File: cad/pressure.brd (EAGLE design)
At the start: 47.9 x 64.8 mm, 14 parts, among them U1 WEMOS-D1-MINI, U2 ABPSENSOR, U3 BATTERY-CHARGER-LI-PROT

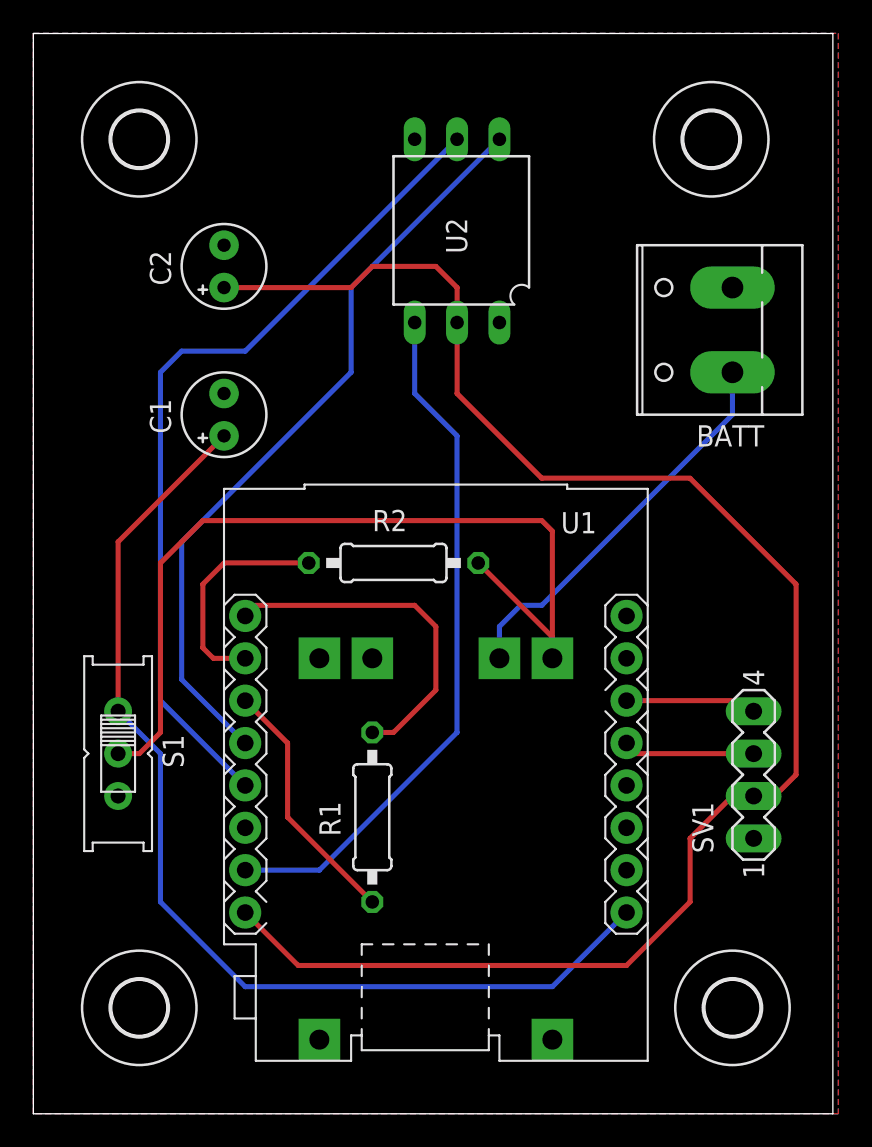
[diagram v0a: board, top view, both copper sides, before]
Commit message: Added pressure sensor settings to status
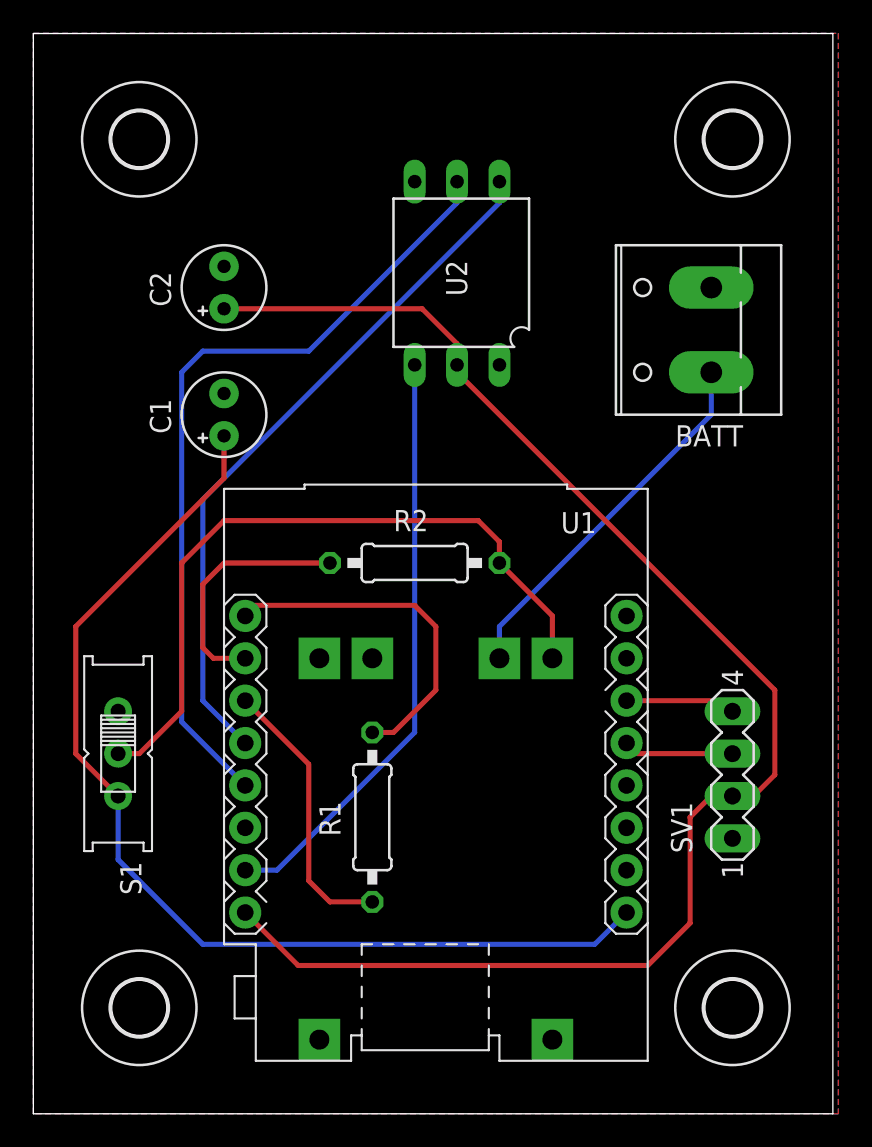
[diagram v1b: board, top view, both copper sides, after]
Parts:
- moved U2 2.54 mm to (38.1, 53.3)
- moved BATT 1.27 mm to (52.1, 48.3)
- moved C2 1.27 mm to (22.9, 50.8)
- moved U$3 1.27 mm to (53.3, 59.7)
- moved R2 1.27 mm to (34.3, 34.3)
- moved SV1 1.27 mm to (53.3, 21.6)
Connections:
- net +5V: now also S1.S; no longer S1.O
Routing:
- net N$10: track 53.2 -> 42.7 mm
- net +3V3: track 99.2 -> 90.1 mm
- net N$4: track 41.7 -> 35.6 mm
- net N$2: track 45.7 -> 42.1 mm
- net N$1: track 50.4 -> 48.3 mm
- net N$6: track 15.2 -> 16.7 mm
- net N$9: track 13.5 -> 14.8 mm
- net N$8: track 23.7 -> 22.4 mm
- net N$5: track 7.88 -> 6.61 mm
- net N$3: track 7.88 -> 6.61 mm
